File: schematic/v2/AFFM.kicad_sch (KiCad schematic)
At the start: 34 parts, among them J13 STEREO_OUT, J14 STEREO_IN, K1 DIPxx-1Axx-11x, K2 DIPxx-1Axx-11x, K3 DIPxx-1Axx-11x, K4 DIPxx-1Axx-11x

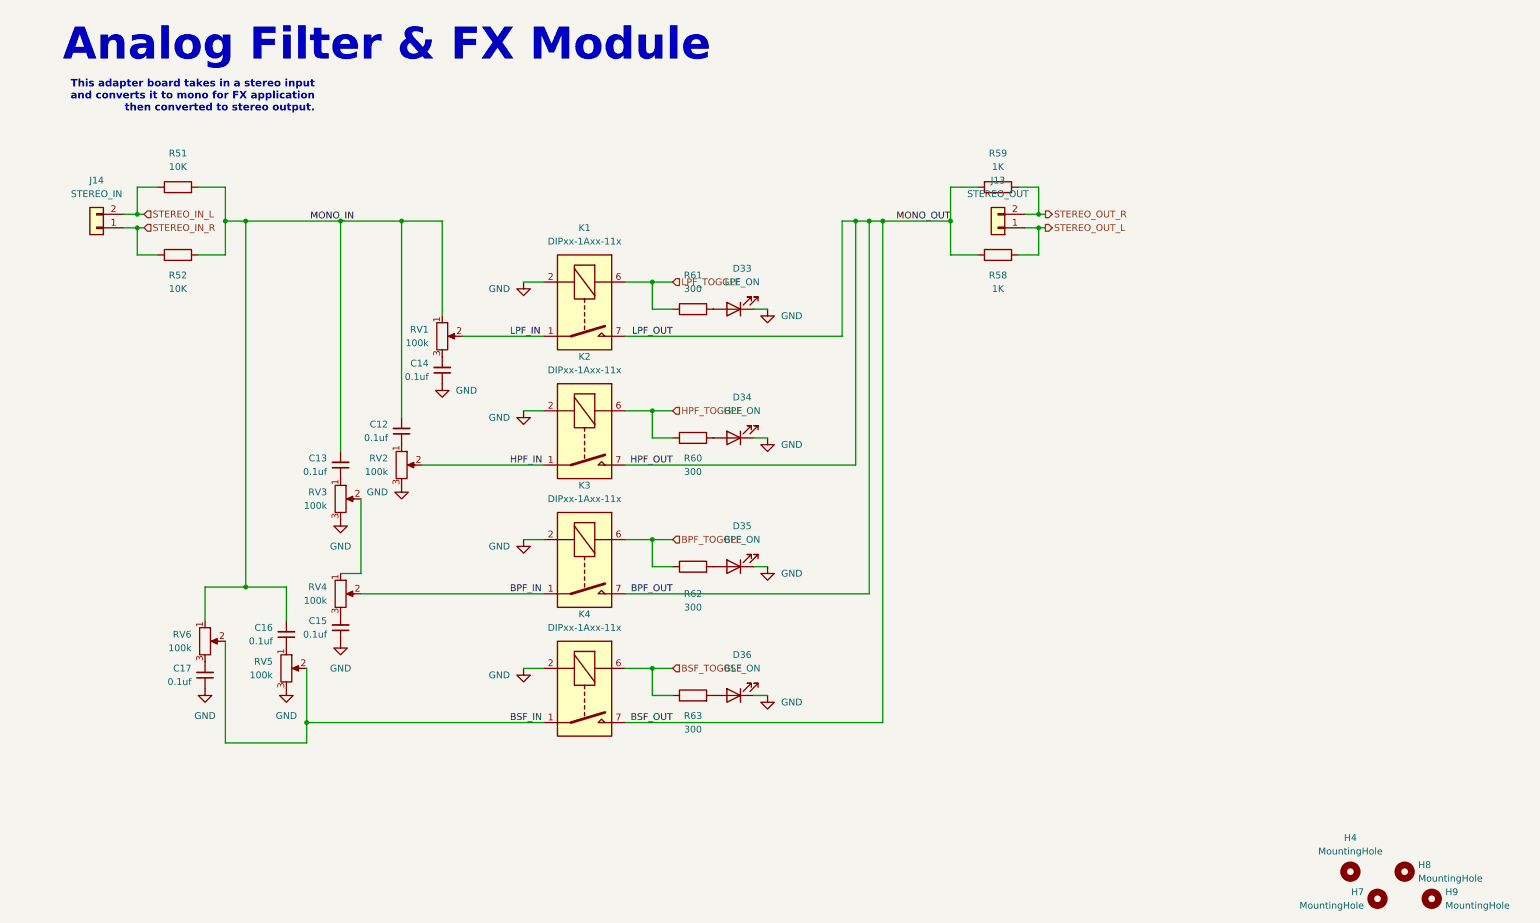
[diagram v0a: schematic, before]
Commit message: dip switch for multi pole filter? this is all for experimenting for now, a refined design with less togleables will come later
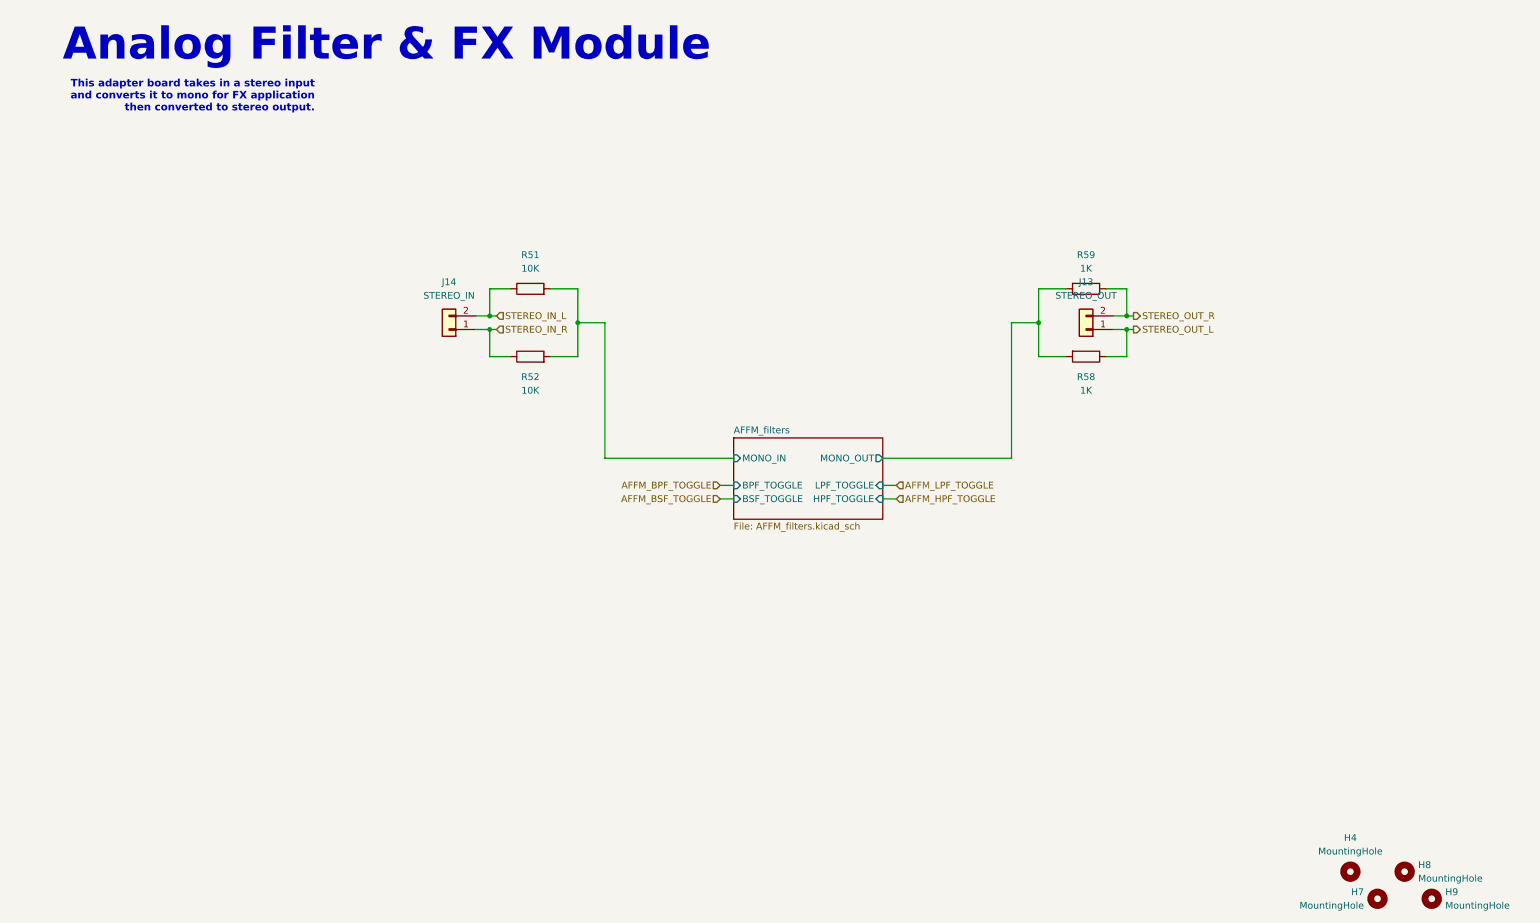
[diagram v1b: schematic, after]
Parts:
- removed C12, C13, C14, C15, C16, C17: 0.1uf, Capacitor_SMD:C_0805_2012Metric, symbol Device:C_Small
- removed D33: LPF_ON, LED_SMD:LED_0603_1608Metric, symbol Device:LED
- removed D34: HPF_ON, LED_SMD:LED_0603_1608Metric, symbol Device:LED
- removed D35: BPF_ON, LED_SMD:LED_0603_1608Metric, symbol Device:LED
- removed D36: BSF_ON, LED_SMD:LED_0603_1608Metric, symbol Device:LED
- removed K1, K2, K3, K4: DIPxx-1Axx-11x, Relay_THT:Relay_StandexMeder_DIP_LowProfile, symbol Relay:DIPxx-1Axx-11x
- removed R60, R61, R62, R63: 300, Resistor_SMD:R_0805_2012Metric_Pad1.20x1.40mm_HandSolder, symbol Device:R
- removed RV1, RV2, RV3, RV4, RV5, RV6: 100k, Potentiometer_THT:Potentiometer_Alps_RK09Y11_Single_Horizontal, symbol Device:R_Potentiometer
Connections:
- net BPF_OUT renamed AFFM_filters/MONO_OUT
- net MONO_IN renamed AFFM_filters/MONO_IN
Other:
- added sheet AFFM_filters (AFFM_filters.kicad_sch)
- moved on the sheet: J13, J14, R51, R52, R58, R59

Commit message: some progress on affm board
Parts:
- added J16: 12V-, Connector:Banana_Jack_1Pin, symbol Connector:Conn_01x01_Socket
- added J17: GND, Connector:Banana_Jack_1Pin, symbol Connector:Conn_01x01_Socket
- added J19: 12V+, Connector:Banana_Jack_1Pin, symbol Connector:Conn_01x01_Socket
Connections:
- new net AFFM_filters/V+: J19.1 (Pin_1)
- new net AFFM_filters/V-: J17.1 (Pin_1)
- no-connect marks 0 -> 1
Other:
- sheet AFFM_filters ports: added V+, V-; removed none

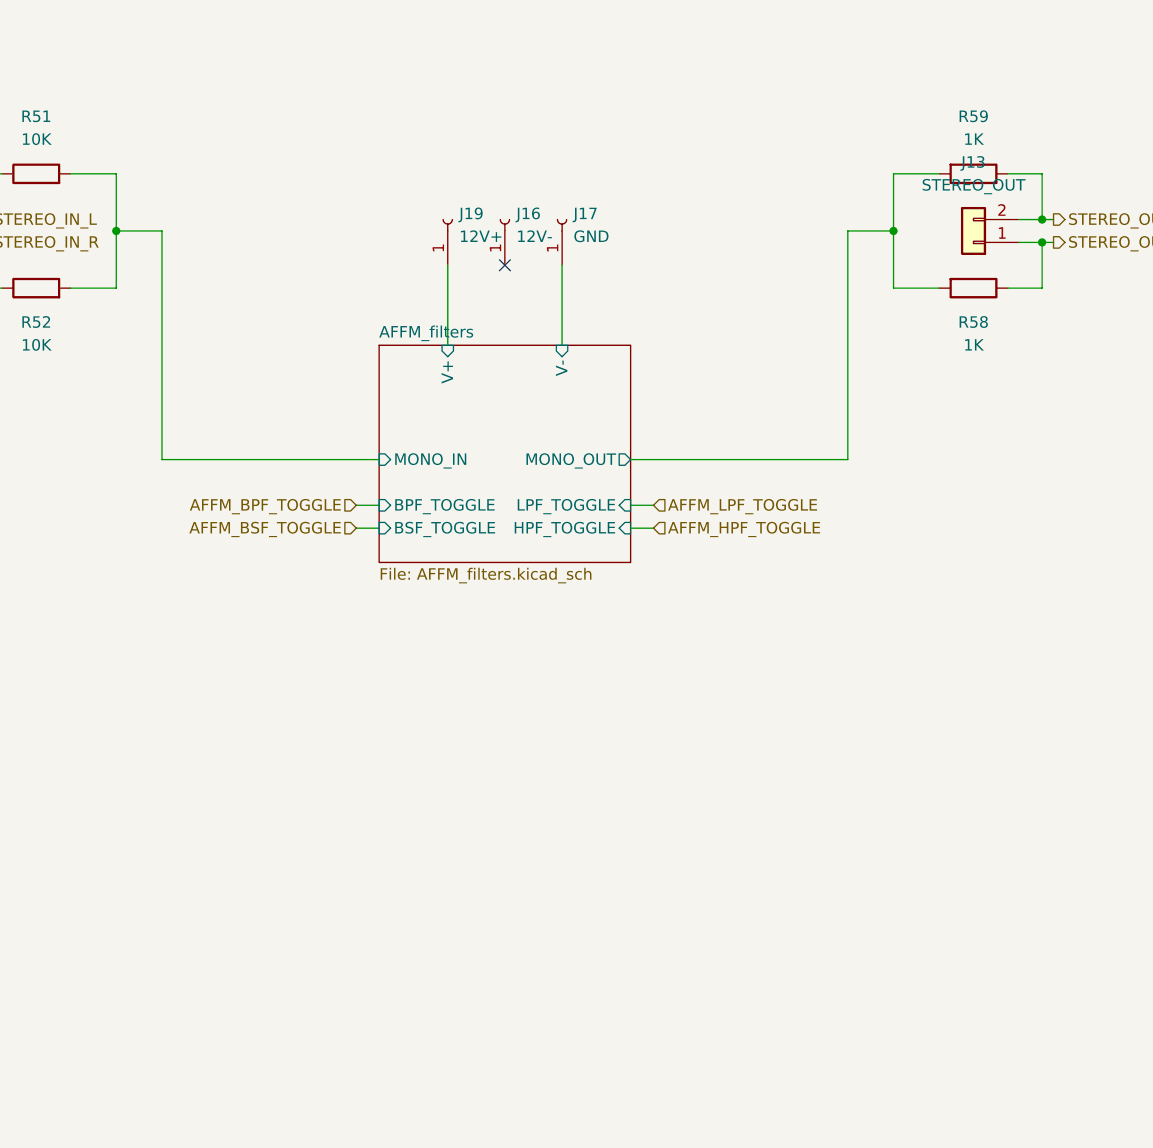
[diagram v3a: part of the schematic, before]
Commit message: now making a v3 with HATs for each nucleo with my needed shit. this will make things very compact and hopefully much cheaper
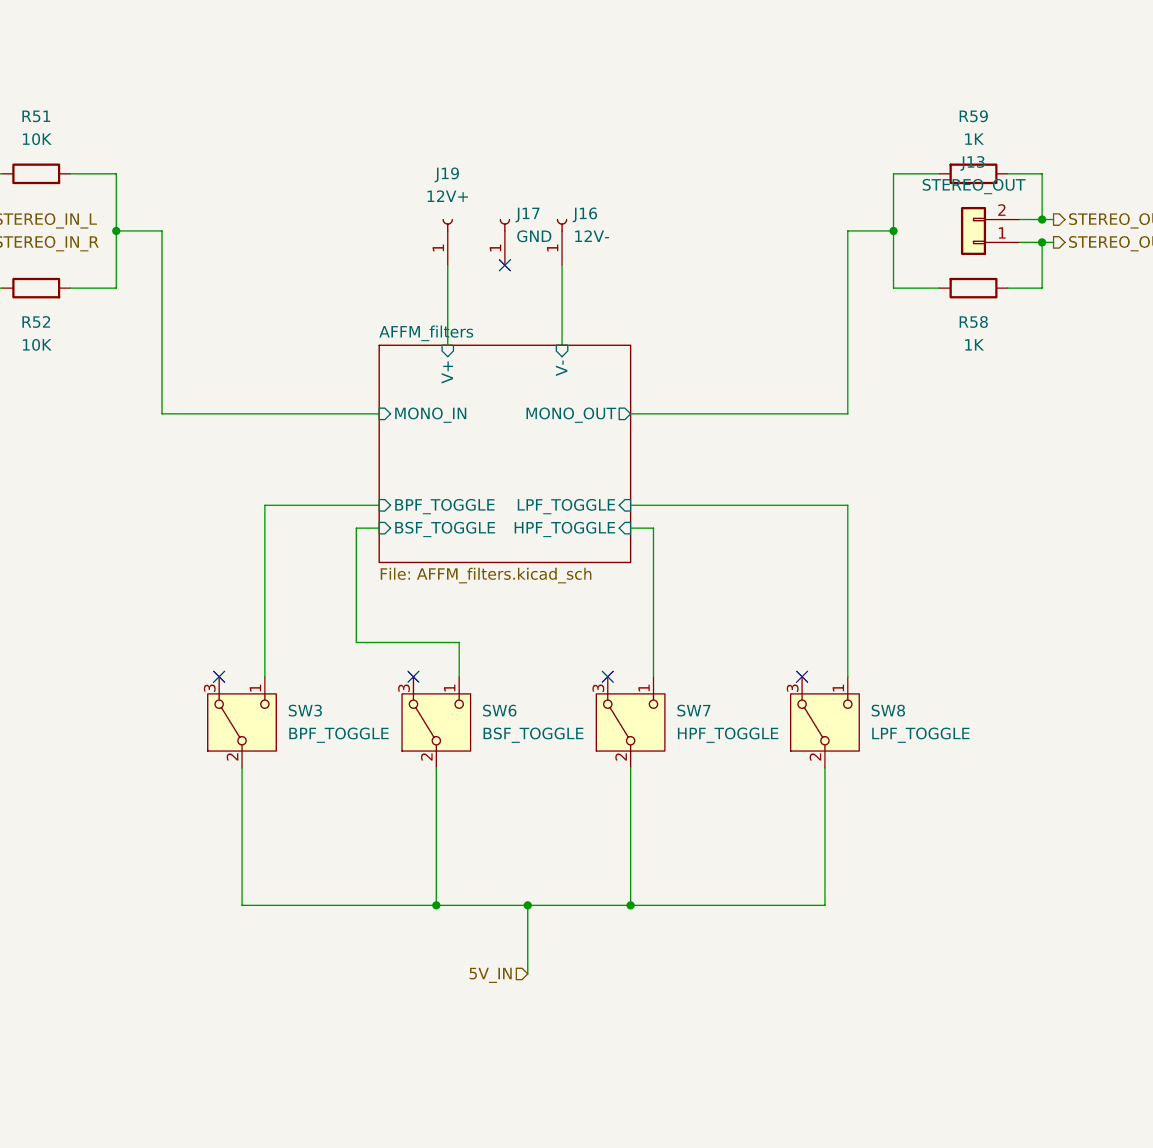
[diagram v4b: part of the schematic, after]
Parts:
- added SW3: BPF_TOGGLE, Button_Switch_SMD:Nidec_Copal_CAS-120A, symbol Switch:SW_Nidec_CAS-120A1
- added SW6: BSF_TOGGLE, Button_Switch_SMD:Nidec_Copal_CAS-120A, symbol Switch:SW_Nidec_CAS-120A1
- added SW7: HPF_TOGGLE, Button_Switch_SMD:Nidec_Copal_CAS-120A, symbol Switch:SW_Nidec_CAS-120A1
- added SW8: LPF_TOGGLE, Button_Switch_SMD:Nidec_Copal_CAS-120A, symbol Switch:SW_Nidec_CAS-120A1
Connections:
- net AFFM_filters/V-: now also J16.1 (Pin_1); no longer J17.1 (Pin_1)
- new net 5V_IN: SW3.2 (B), SW6.2 (B), SW7.2 (B), SW8.2 (B)
- new net AFFM_filters/BPF_TOGGLE: SW3.1 (C)
- new net AFFM_filters/BSF_TOGGLE: SW6.1 (C)
- new net AFFM_filters/HPF_TOGGLE: SW7.1 (C)
- new net AFFM_filters/LPF_TOGGLE: SW8.1 (C)
- no-connect marks 1 -> 5
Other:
- moved on the sheet: J16, J17
